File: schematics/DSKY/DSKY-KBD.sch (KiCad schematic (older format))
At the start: 62 parts, among them SW1 SW_Push, SW10 SW_Push, SW11 SW_Push, SW12 SW_Push, SW13 SW_Push, SW14 SW_Push, SW15 SW_Push, SW16 SW_Push, SW17 SW_Push, SW18 SW_Push, SW19 SW_Push, SW2 SW_Push, SW3 SW_Push, SW4 SW_Push, SW5 SW_Push, SW6 SW_Push, SW7 SW_Push, SW8 SW_Push, SW9 SW_Push, U1 74LS273, U10 74LS20, U11 74LS20, U12 74LS20, U13 74LS02, U14 74LS27, U15 74LS27, U16 74LS74, U18 74LS00, U2 74LS244, U3 LM555, U4 74LS04, U40 74LS32, U47 74LS126, U5 74LS04, U6 74LS00, U8 74LS10, U9 74LS20

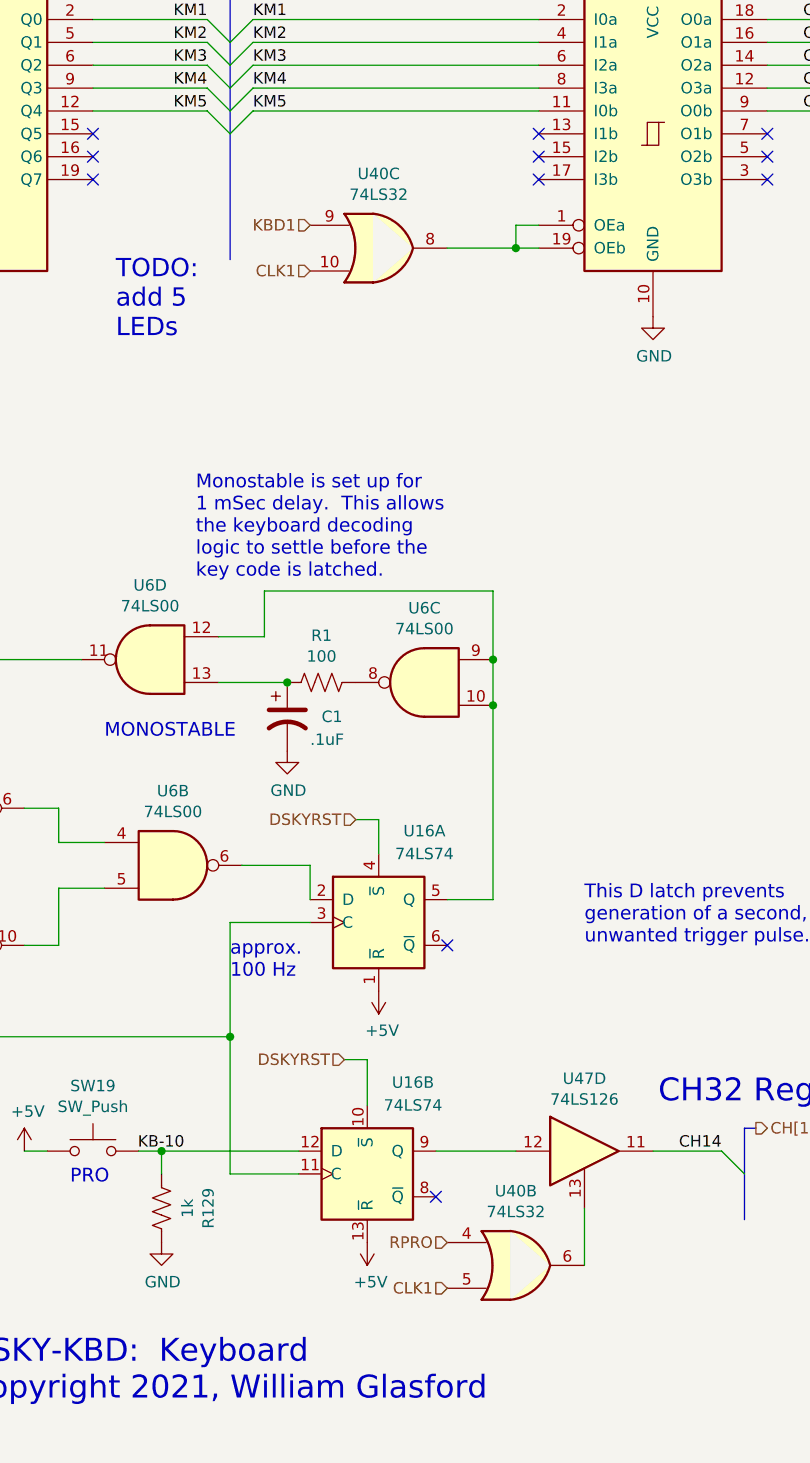
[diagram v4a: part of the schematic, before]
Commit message: Sign processing overhauled.
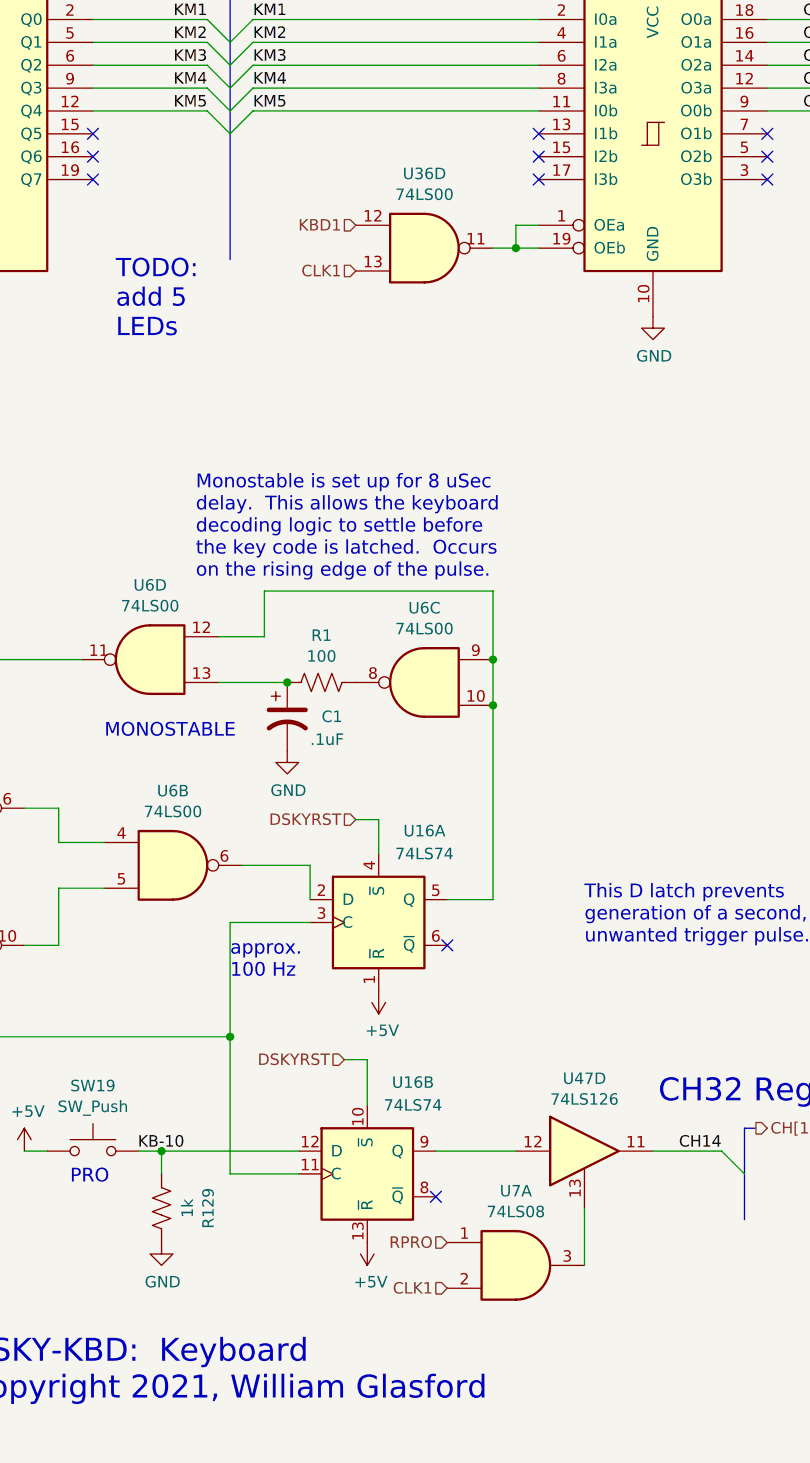
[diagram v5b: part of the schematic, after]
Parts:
- removed U40: 74LS32, symbol 74xx:74LS32
- added U36: 74LS00, symbol 74xx:74LS00
- added U7: 74LS08, symbol 74xx:74LS08
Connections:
- net CLK1: now also U36.13, U7.2
- net KBD1: now also U36.12
- net RPRO: now also U7.1
- net at U47.13: now also U7.3
- net at U2.1 (OEa), U2.19 (OEb): now also U36.11
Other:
- note added: "Monostable is set up for 8 uSec \ndelay. This allows the keyboard \ndecoding logic to settle before \nthe key code is latched. Occurs\non the rising edge of the pulse."
- note removed: "Monostable is set up for\n1 mSec delay. This allows\nthe keyboard decoding\nlogic to settle before the\nkey code is latched."
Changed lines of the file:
@@
 $Descr A 11000 8500
 encoding utf-8
-Sheet 10 10
+Sheet 10 11
 Title ""
 Date ""
@@
 MONOSTABLE
 Text Notes 7550 3600 0    60   ~ 0
-Monostable is set up for\n1 mSec delay.  This allows\nthe keyboard decoding\nlogic to settle before the\nkey code is latched.
+Monostable is set up for 8 uSec \ndelay.  This allows the keyboard \ndecoding logic to settle before \nthe key code is latched.  Occurs\non the rising edge of the pulse.
 Wire Wire Line
 	2500 1100 2600 1100
@@
 	1    0    0    -1
 $EndComp
-$Comp
-L 74xx:74LS32 U?
-U 3 1 678085A4
-P 8350 2150
-AR Path="/60F98A1A/678085A4" Ref="U?"  Part="2"
-AR Path="/66BEEA04/678085A4" Ref="U?"  Part="2"
-AR Path="/60F98A72/66CE2FA0/678085A4" Ref="U?"  Part="2"
-AR Path="/60F98A72/66CE2F9E/678085A4" Ref="U?"  Part="2"
-AR Path="/60F98A72/678085A4" Ref="U40"  Part="3"
-F 0 "U40" H 8350 2475 50  0000 C CNN
-F 1 "74LS32" H 8350 2384 50  0000 C CNN
-F 2 "" H 8350 2150 50  0001 C CNN
-F 3 "http://www.ti.com/lit/gpn/sn74LS32" H 8350 2150 50  0001 C CNN
-	3    8350 2150
-	1    0    0    -1
-$EndComp
-Wire Wire Line
-	8650 2150 8950 2150
+Wire Wire Line
+	8850 2150 8950 2150
 Wire Wire Line
 	8950 2150 9050 2150
@@
 Wire Wire Line
 	8950 2050 8950 2150
-Text HLabel 8050 2050 0    50   Input ~ 0
+Text HLabel 8250 2050 0    50   Input ~ 0
 KBD1
-Text HLabel 8050 2250 0    50   Input ~ 0
+Text HLabel 8250 2250 0    50   Input ~ 0
 CLK1
 Text Notes 9450 850  2    100  ~ 0
@@
 	1    0    0    -1
 $EndComp
-$Comp
-L 74xx:74LS32 U?
-U 2 1 62A6291C
-P 8950 6600
-AR Path="/60F98A1A/62A6291C" Ref="U?"  Part="2"
-AR Path="/66BEEA04/62A6291C" Ref="U?"  Part="2"
-AR Path="/60F98A72/66CE2FA0/62A6291C" Ref="U?"  Part="2"
-AR Path="/60F98A72/66CE2F9E/62A6291C" Ref="U?"  Part="2"
-AR Path="/60F98A72/62A6291C" Ref="U40"  Part="2"
-F 0 "U40" H 8950 6925 50  0000 C CNN
-F 1 "74LS32" H 8950 6834 50  0000 C CNN
-F 2 "" H 8950 6600 50  0001 C CNN
-F 3 "http://www.ti.com/lit/gpn/sn74LS32" H 8950 6600 50  0001 C CNN
-	2    8950 6600
-	1    0    0    -1
-$EndComp
 Wire Wire Line
 	8600 6100 8950 6100
 Text HLabel 8650 6500 0    50   Input ~ 0
 RPRO
-Text HLabel 8650 6700 0    50   Input ~ 0
-CLK1
 Wire Wire Line
 	9250 6350 9250 6600
@@
 Wire Wire Line
 	8350 4650 8350 4800
+$Comp
+L 74xx:74LS00 U18
+U 4 1 614FF2D5
+P 3500 1400
+F 0 "U18" H 3700 1700 50  0000 C CNN
+F 1 "74LS00" H 3700 1600 50  0000 C CNN
+F 2 "" H 3500 1400 50  0001 C CNN
+F 3 "http://www.ti.com/lit/gpn/sn74ls00" H 3500 1400 50  0001 C CNN
+	4    3500 1400
+	1    0    0    -1
+$EndComp
+$Comp
+L 74xx:74LS00 U36
+U 4 1 61A0A316
+P 8550 2150
+F 0 "U36" H 8550 2475 50  0000 C CNN
+F 1 "74LS00" H 8550 2384 50  0000 C CNN
+F 2 "" H 8550 2150 50  0001 C CNN
+F 3 "http://www.ti.com/lit/gpn/sn74ls00" H 8550 2150 50  0001 C CNN
+	4    8550 2150
+	1    0    0    -1
+$EndComp
+$Comp
+L 74xx:74LS08 U7
+U 1 1 61B1881C
+P 8950 6600
+F 0 "U7" H 8950 6925 50  0000 C CNN
+F 1 "74LS08" H 8950 6834 50  0000 C CNN
+F 2 "" H 8950 6600 50  0001 C CNN
+F 3 "http://www.ti.com/lit/gpn/sn74LS08" H 8950 6600 50  0001 C CNN
+	1    8950 6600
+	1    0    0    -1
+$EndComp
 Wire Bus Line
 	9950 6000 9950 6400
@@
 Wire Bus Line
 	2800 650  2800 7400
-$Comp
-L 74xx:74LS00 U18
-U 4 1 614FF2D5
-P 3500 1400
-F 0 "U18" H 3700 1700 50  0000 C CNN
-F 1 "74LS00" H 3700 1600 50  0000 C CNN
-F 2 "" H 3500 1400 50  0001 C CNN
-F 3 "http://www.ti.com/lit/gpn/sn74ls00" H 3500 1400 50  0001 C CNN
-	4    3500 1400
-	1    0    0    -1
-$EndComp
+Text HLabel 8650 6700 0    50   Input ~ 0
+CLK1
 $EndSCHEMATC

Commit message: DSKY Redesign
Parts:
- added U19: 74LS04, symbol 74xx:74LS04
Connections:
- net CLK1: now also U36.12; no longer U36.13
- net KBD1: now also U19.3; no longer U36.12
- new net: U19.4, U36.13
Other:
- note removed: "Use 2 9-resister\nnetwork chips."
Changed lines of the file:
@@
 $Descr A 11000 8500
 encoding utf-8
-Sheet 11 12
+Sheet 3 15
 Title ""
 Date ""
@@
 Wire Wire Line
 	8950 2050 8950 2150
+Text HLabel 7650 2650 0    50   Input ~ 0
+KBD1
 Text HLabel 8250 2050 0    50   Input ~ 0
-KBD1
-Text HLabel 8250 2250 0    50   Input ~ 0
 CLK1
 Text Notes 9450 850  2    100  ~ 0
@@
 	2800 7400 1600 7400
 Connection ~ 8950 2150
-Text Notes 7200 2550 0    80   ~ 0
+Text Notes 7250 2200 0    80   ~ 0
 TODO: \nadd 5 \nLEDs
 Wire Bus Line
@@
 Text Notes 6550 7200 0    100  ~ 0
 DSKY-KBD:  Keyboard\nCopyright 2021, William Glasford
-Text Notes 2900 7050 0    80   ~ 0
-Use 2 9-resister\nnetwork chips.
 Wire Wire Line
 	8300 5700 8200 5700
@@
 Text HLabel 8650 6700 0    50   Input ~ 0
 CLK1
+$Comp
+L 74xx:74LS04 U?
+U 2 1 63C2FDE6
+P 7950 2650
+AR Path="/60F989FD/63C2FDE6" Ref="U?"  Part="3"
+AR Path="/60F98A72/63C2FDE6" Ref="U19"  Part="2"
+F 0 "U19" H 7950 2967 50  0000 C CNN
+F 1 "74LS04" H 7950 2876 50  0000 C CNN
+F 2 "" H 7950 2650 50  0001 C CNN
+F 3 "http://www.ti.com/lit/gpn/sn74LS04" H 7950 2650 50  0001 C CNN
+	2    7950 2650
+	1    0    0    -1
+$EndComp
+Wire Wire Line
+	8250 2250 8250 2650
 Wire Bus Line
 	9950 6000 9950 6400
